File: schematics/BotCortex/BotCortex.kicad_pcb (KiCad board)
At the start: 2 copper layers, 60 parts, among them P1 2x Serial, P10 Stepper Upperarm, P11 Stepper Hip, P12 POWER_IN, P13 PowerEnableIn, P14 Power Stepper 2, P15 Power Stepper 3, P16 Power Stepper 4, P17 PowerEnableOut, P18 Power Stepper 5, P19 ODroid Power, P2 Herkulex Servo, P20 POTI 10K, P21 Reset_Conn, P22 Reset Conn, P23 LED-Driver-I2C, P24 UART6, P25 Thermal_Printer, P28 Power Stepper 1, P3 Encoder Socket 0, P4 Encoder Socket, P5 Stepper Elbow, P6 Power In uC Servo 9V, P7 Power Out uC Servo, P8 Stepper Forearm, P9 Stepper Wrist, Q1 BC237, Q2 BC237, SW2 reset, U1 7805, U2 LM7809ACT, U3 LM7809ACT, U4 Teensy_3.5, U5 7803

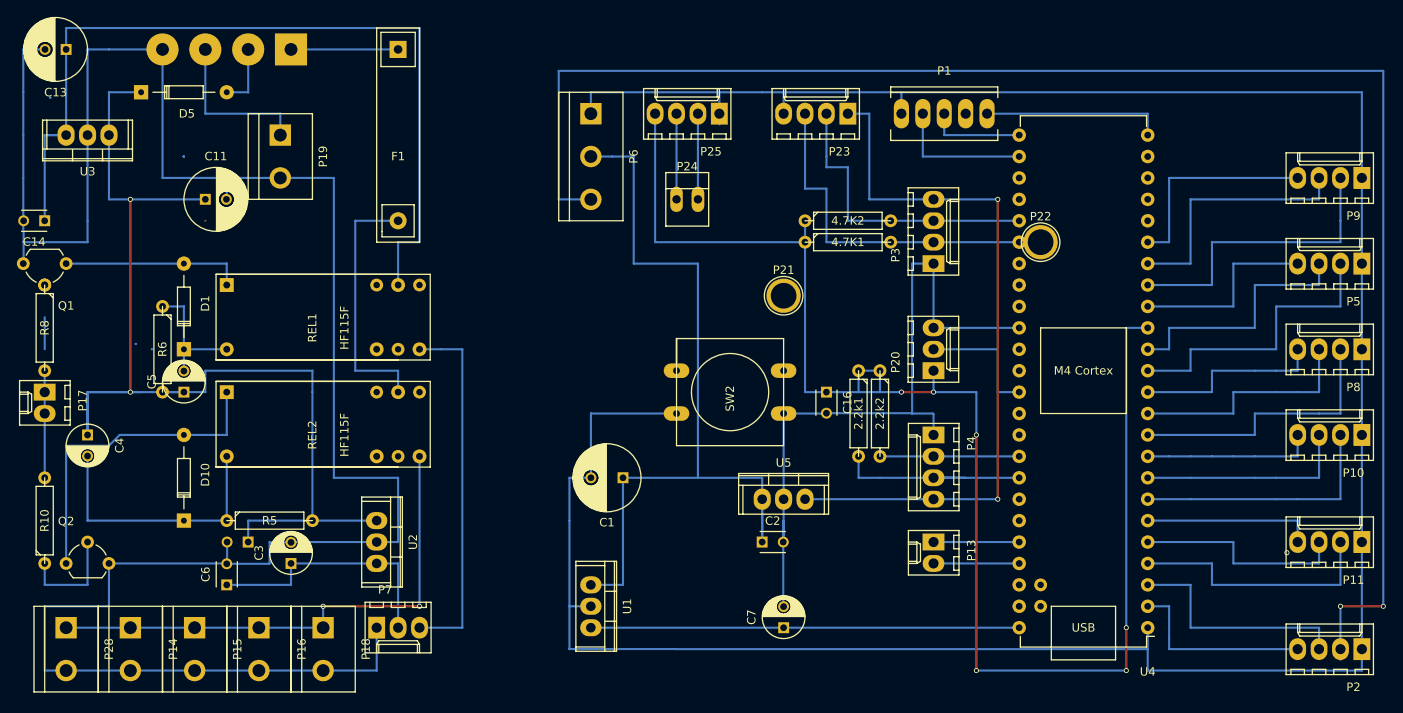
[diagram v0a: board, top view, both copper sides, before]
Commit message: changed pins to have easier pcb
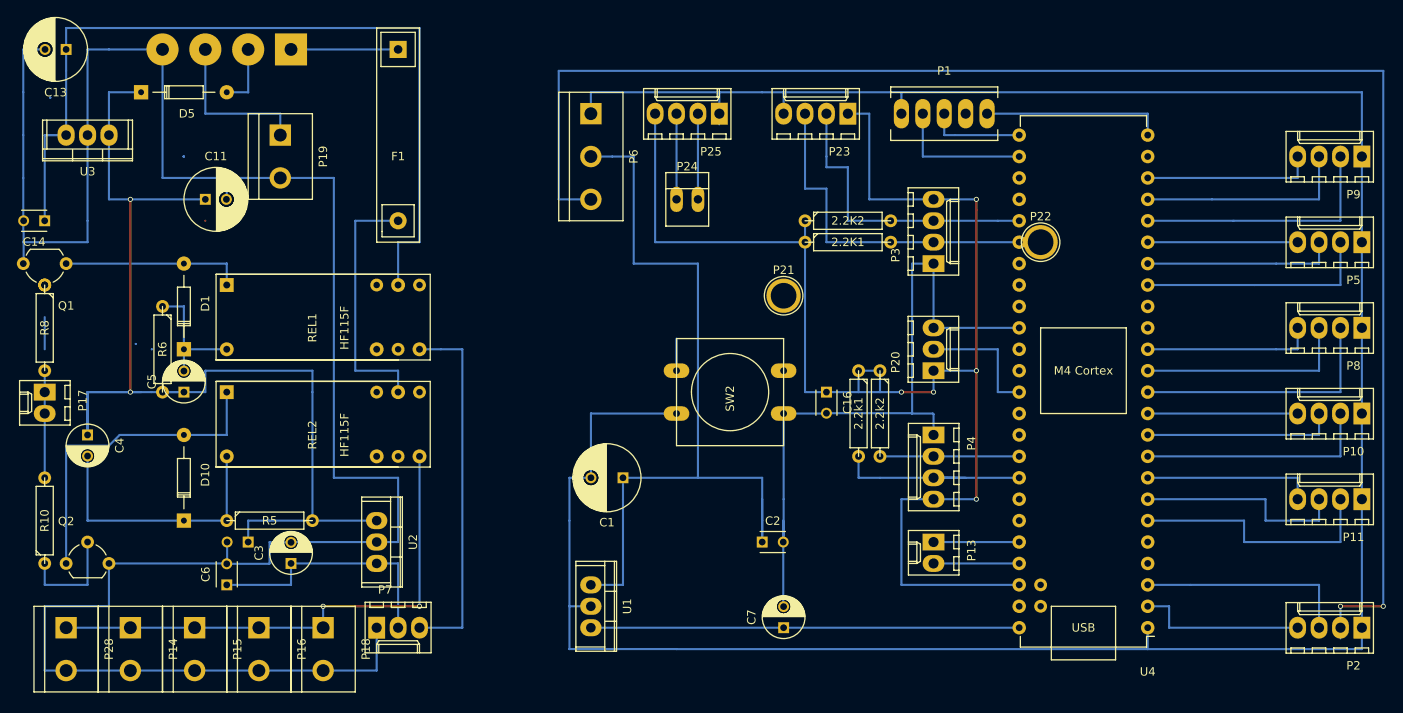
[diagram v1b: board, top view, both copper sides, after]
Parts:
- removed 4.7K1, 4.7K2: R, Discret:R4
- removed U5: 7803, BotCortex:78XX-TO-220
- added 2.2K1: R, Discret:R4, F.Cu at (146.1, 63.5)
- added 2.2K2: R, Discret:R4, F.Cu at (146.1, 61.0)
- moved P11 5.08 mm to (207.0, 94.0)
- moved P10 2.54 mm to (207.0, 83.8)
- moved P2 2.54 mm to (207.0, 109.2)
- moved P5 2.54 mm to (207.0, 63.5)
- moved P8 2.54 mm to (207.0, 73.7)
- moved P9 2.54 mm to (207.0, 53.3)
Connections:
- P23 pad 1: Net-(P23-Pad1) -> /3.3V
- P3 pad 4: Net-(P23-Pad1) -> /3.3V
- P4 pad 4: Net-(P23-Pad1) -> /3.3V
- U4 pad 10: /CLK2 -> /DIR1
- U4 pad 11: /DIR2 -> /EN1
- U4 pad 12: /EN2 -> /CLK2
- U4 pad 13: /CLK3 -> /DIR2
- U4 pad 14: /DIR3 -> /EN2
- U4 pad 15: /3.3V -> (no net)
- U4 pad 16: /EN3 -> (no net)
- U4 pad 17: /CLK4 -> /CLK3
- U4 pad 18: /DIR4 -> /DIR3
- U4 pad 19: /EN4 -> /EN3
- U4 pad 20: (no net) -> /CLK4
- U4 pad 21: (no net) -> /DIR4
- U4 pad 22: (no net) -> /EN4
- U4 pad 4: /CLK0 -> (no net)
- U4 pad 46: (no net) -> /3.3V
- U4 pad 5: /DIR0 -> (no net)
- U4 pad 6: /En0 -> /CLK0
- U4 pad 7: /CLK1 -> /DIR0
- U4 pad 8: /DIR1 -> /En0
- U4 pad 9: /EN1 -> /CLK1
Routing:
- net Net-(P23-Pad1): track 86.4 -> 0.00 mm, vias 2 -> 0
- net /DIR3: track 30.5 -> 22.9 mm
- net /CLK3: track 35.6 -> 27.9 mm
- net GNDPWR: track 659.4 -> 654.3 mm
- net /DIR4: track 30.5 -> 25.4 mm
- net /EN4: track 25.4 -> 20.3 mm
- net /EN3: track 22.9 -> 17.8 mm
- net /CLK4: track 35.6 -> 30.5 mm
- net /VDDServo9V: track 191.8 -> 189.2 mm
- net Net-(P2-Pad4): track 22.9 -> 20.3 mm
- net Net-(P2-Pad3): track 27.9 -> 25.4 mm
- net /EN1: track 20.3 -> 17.8 mm
- net /EN2: track 22.9 -> 20.3 mm
- net /DIR2: track 27.9 -> 25.4 mm
- net /DIR1: track 25.4 -> 22.9 mm
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
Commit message: Currrently making the teensy pcb
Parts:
- moved P6 20.5 mm to (118.1, 73.7)
- moved C1 10.8 mm to (127.0, 99.1), turned to 0 degrees
- moved P4 7.73 mm to (157.5, 94.0), turned to 90 degrees
- moved P22 3.81 mm to (172.7, 63.5)
- moved 2.2k1 2.54 mm to (147.3, 86.4)
- moved 2.2k2 2.54 mm to (149.9, 86.4)
- moved P24 2.54 mm to (124.5, 58.4)
- moved P25 2.54 mm to (128.3, 48.3)
- moved P23 1.27 mm to (144.8, 48.3)
- moved U1 1.27 mm to (116.8, 106.7)
- moved P10 1.27 mm to (205.7, 83.8)
- moved P11 1.27 mm to (205.7, 94.0)
- moved P13 1.27 mm to (157.5, 99.1)
- moved P2 1.27 mm to (205.7, 109.2)
- moved P20 1.27 mm to (157.5, 78.7)
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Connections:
- U4 pad 2: Net-(P2-Pad4) -> Net-(P2-Pad3)
- U4 pad 3: Net-(P2-Pad3) -> Net-(P2-Pad4)
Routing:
- net GNDPWR: track 654.3 -> 709.1 mm
- net /VDDServo9V: track 189.2 -> 203.2 mm
- net /VDD_uC_5V: track 127.0 -> 118.1 mm
- net /SDA1: track 40.6 -> 47.0 mm
- net /SCl0: track 24.2 -> 30.5 mm, vias 0 -> 2
- net /SDA0: track 16.5 -> 20.3 mm
- net /DIR4: track 25.4 -> 22.9 mm
- net /DIR3: track 22.9 -> 20.3 mm
- net /DIR2: track 25.4 -> 22.9 mm
- net /DIR1: track 22.9 -> 20.3 mm
- net /DIR0: track 26.7 -> 24.1 mm
- net /CLK4: track 30.5 -> 27.9 mm
- net /CLK3: track 27.9 -> 25.4 mm
- net /CLK2: track 30.5 -> 27.9 mm
- net /CLK1: track 27.9 -> 25.4 mm
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
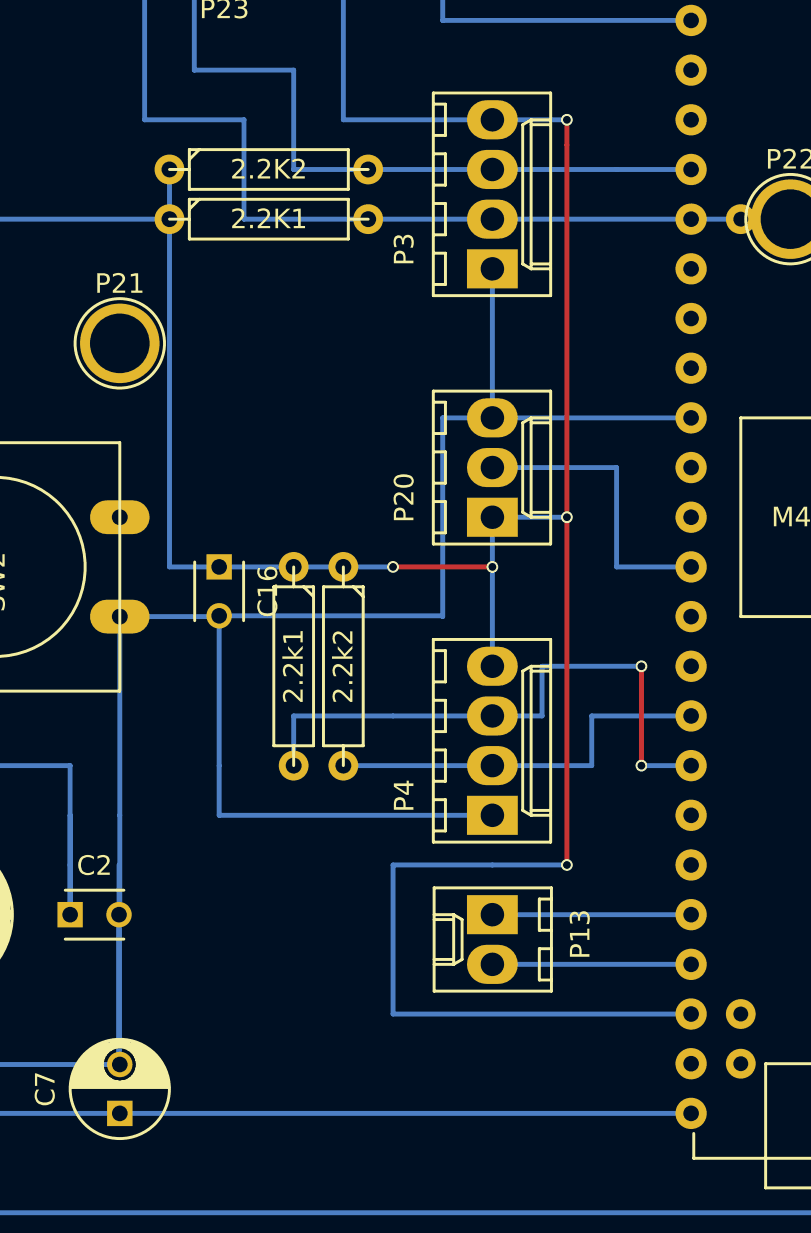
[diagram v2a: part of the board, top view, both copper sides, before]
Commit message: AS5048 require 5V, 3.3 V is not stable. PCB changed.
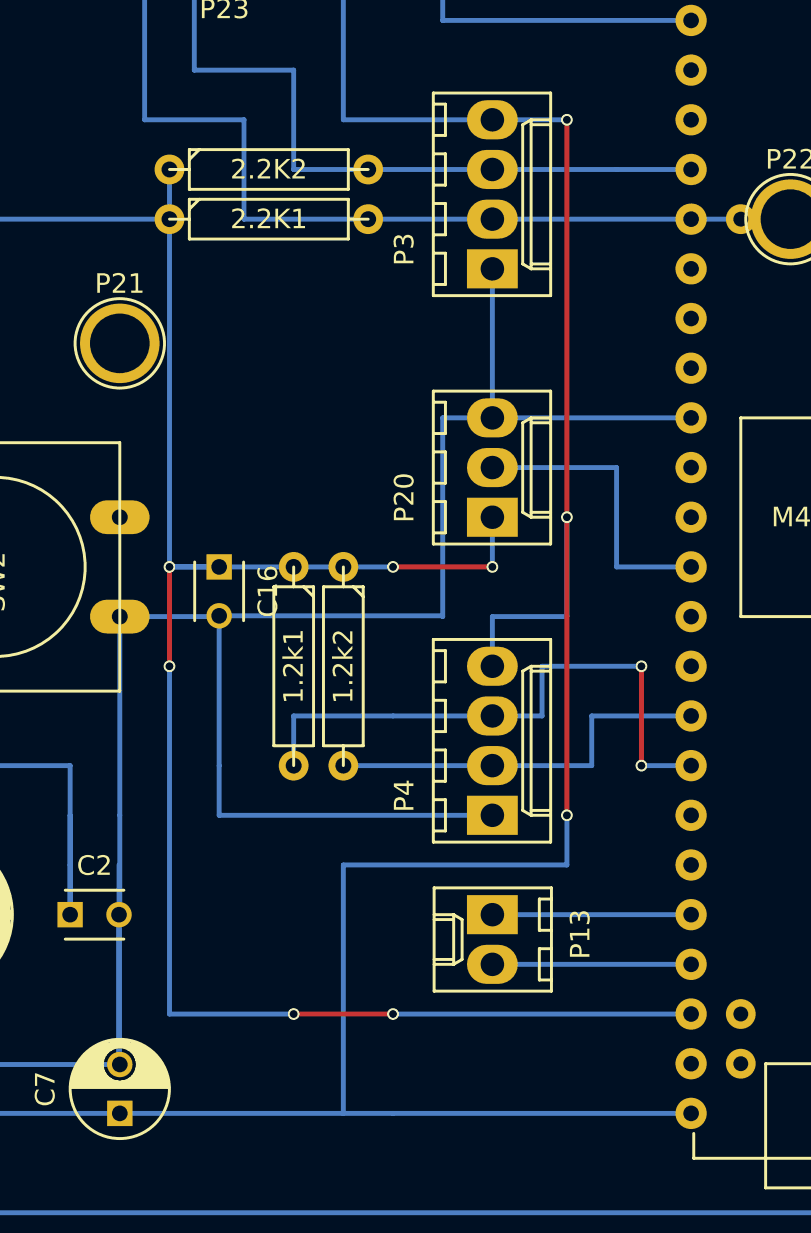
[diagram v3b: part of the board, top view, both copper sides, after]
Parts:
- removed 2.2k1, 2.2k2: R, Discret:R4
- added 1.2k1: R, Discret:R4, F.Cu at (147.3, 86.4)
- added 1.2k2: R, Discret:R4, F.Cu at (149.9, 86.4)
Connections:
- P23 pad 1: /3.3V -> /+5V
- P3 pad 4: /3.3V -> /+5V
- P4 pad 4: /3.3V -> /+5V
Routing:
- net /+5V: track 50.8 -> 151.1 mm, vias 0 -> 3
- net /3.3V: track 180.3 -> 127.0 mm, vias 5 -> 6
